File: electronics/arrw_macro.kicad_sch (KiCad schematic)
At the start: 23 parts, among them J7 Conn_01x05_Female, J8 Conn_01x05_Male, SW59 SW_SPST, SW60 SW_SPST, SW61 SW_SPST, SW62 SW_SPST, SW63 SW_SPST, SW64 SW_SPST, SW65 SW_SPST, SW66 SW_SPST, SW67 SW_SPST, SW68 SW_SPST, U4 PCA9675PW

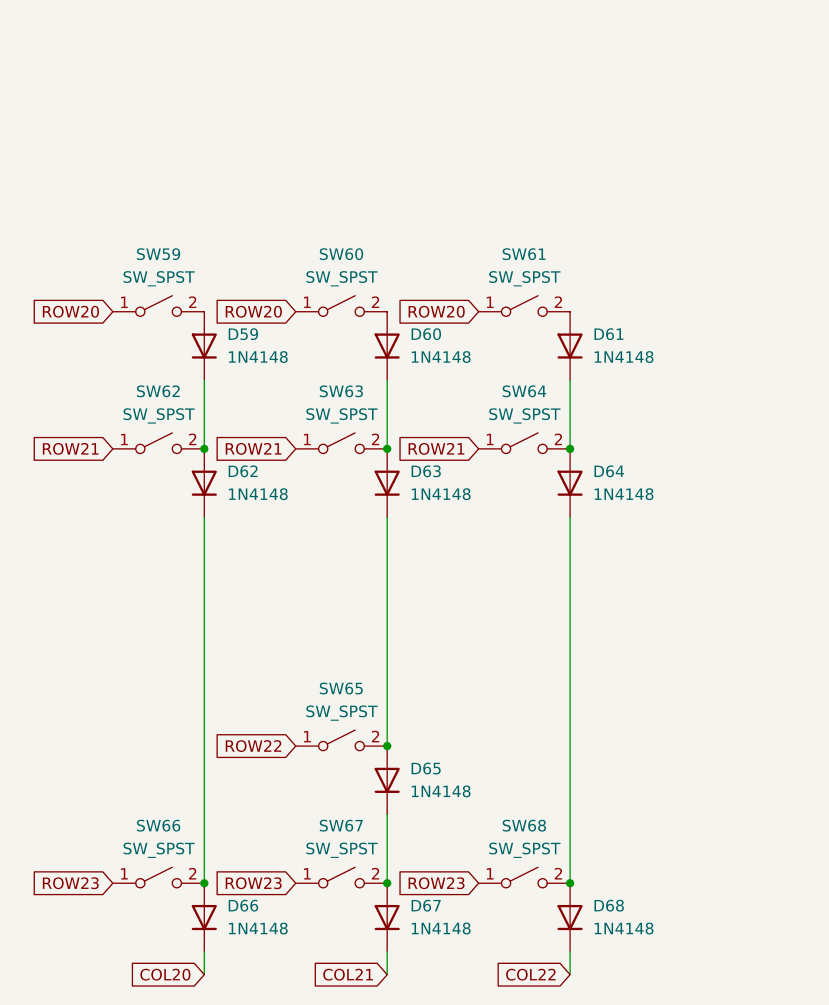
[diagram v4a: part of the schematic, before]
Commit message: fix arrow matrix
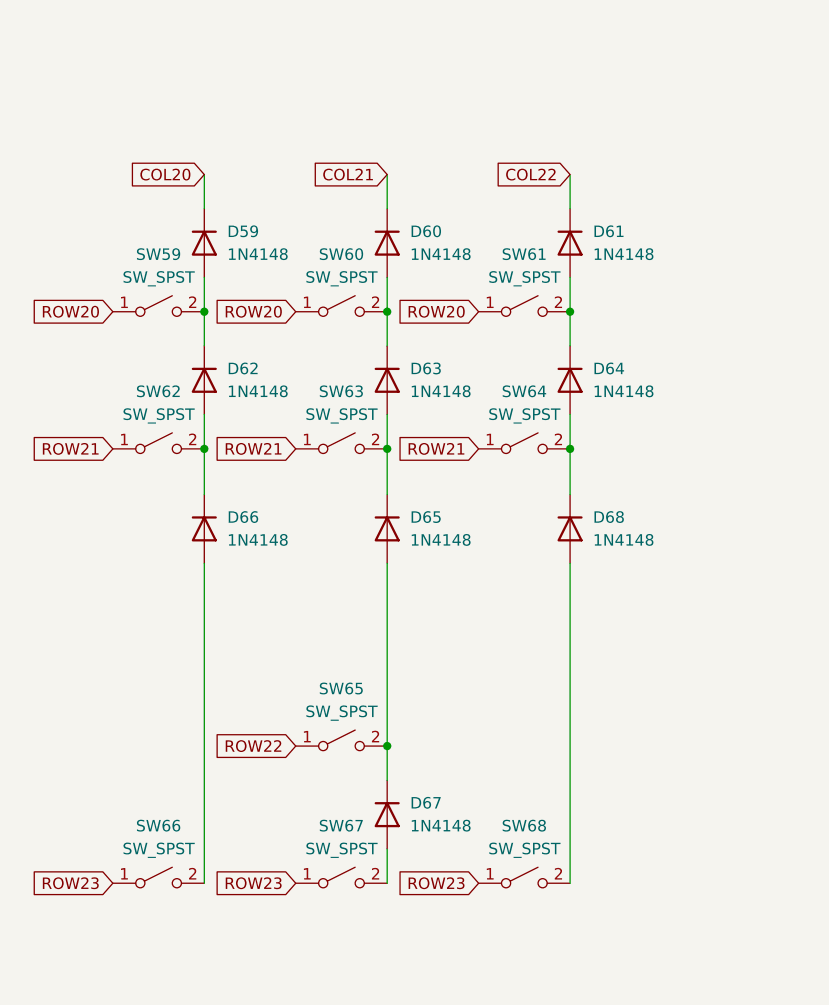
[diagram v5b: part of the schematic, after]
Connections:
- net COL20: now also D59.1 (K); no longer D66.1 (K)
- net COL21: now also D60.1 (K); no longer D67.1 (K)
- net COL22: now also D61.1 (K); no longer D68.1 (K)
- net at D65.2 (A), SW65.2 (B): now also D67.1 (K); no longer D63.1 (K)
- net at D67.2 (A), SW67.2 (B): no longer D65.1 (K)
- net at D63.2 (A), SW63.2 (B): now also D65.1 (K); no longer D60.1 (K)
- net at D60.2 (A), SW60.2 (B): now also D63.1 (K)
- net at D68.2 (A), SW68.2 (B): no longer D64.1 (K)
- net at D64.2 (A), SW64.2 (B): now also D68.1 (K); no longer D61.1 (K)
- net at D61.2 (A), SW61.2 (B): now also D64.1 (K)
- net at D59.2 (A), SW59.2 (B): now also D62.1 (K)
- net at D62.2 (A), SW62.2 (B): now also D66.1 (K); no longer D59.1 (K)
- net at D66.2 (A), SW66.2 (B): no longer D62.1 (K)
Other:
- moved on the sheet: D59, D60, D61, D62, D63, D64, D65, D66, D67, D68

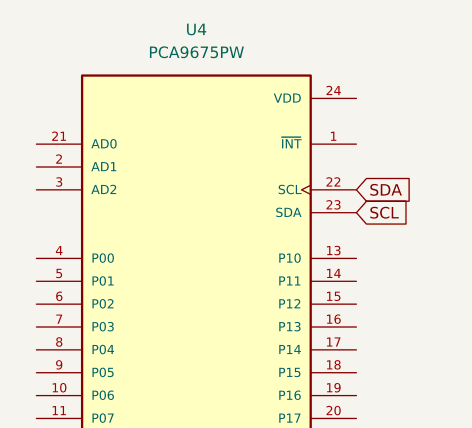
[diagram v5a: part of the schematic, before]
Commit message: fix arrow matrix
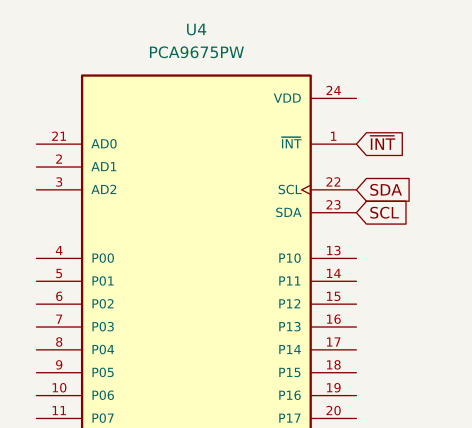
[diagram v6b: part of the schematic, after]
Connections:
- net ~{INT}: now also U4.1 (~{INT})
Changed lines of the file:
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@@
+    )
+  )
+  (global_label "~{INT}" (shape input) (at 224.79 41.91 0) (fields_autoplaced)
+    (effects (font (size 1.27 1.27)) (justify left))
+    (property "Intersheet References" "${INTERSHEET_REFS}" (id 0) (at 230.106 41.9894 0)
+      (effects (font (size 1.27 1.27)) (justify left) hide)
     )
   )

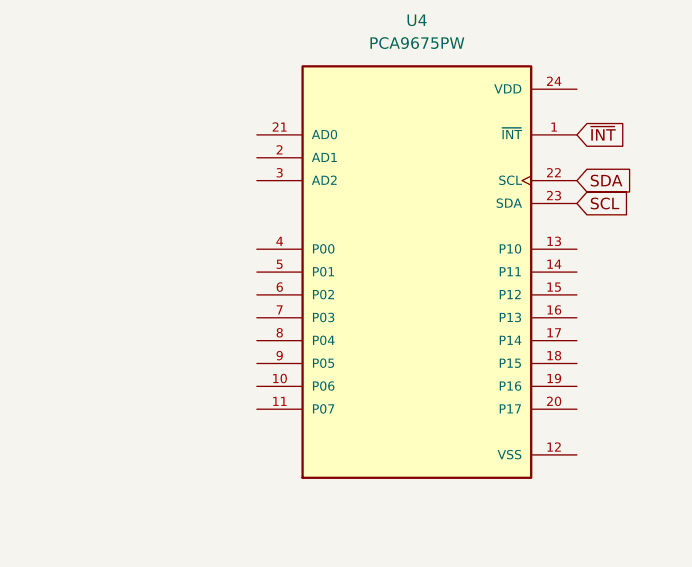
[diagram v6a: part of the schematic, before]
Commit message: connect matrix to io expander
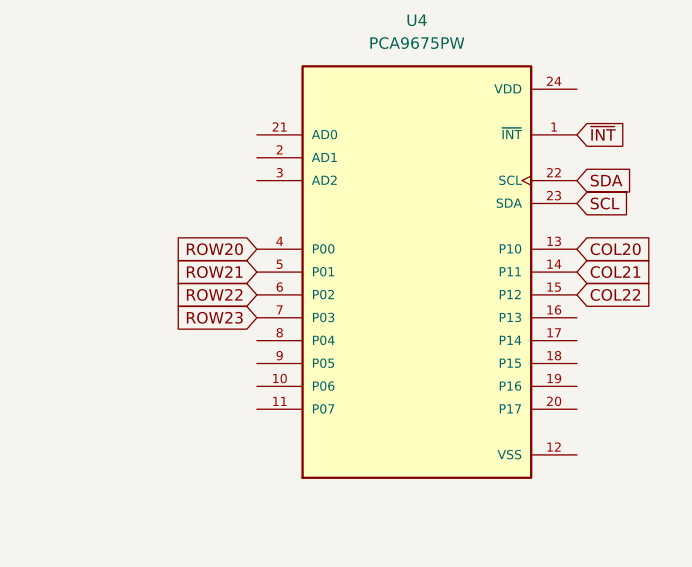
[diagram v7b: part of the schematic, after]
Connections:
- net COL20: now also U4.13 (P10)
- net COL21: now also U4.14 (P11)
- net COL22: now also U4.15 (P12)
- net ROW20: now also U4.4 (P00)
- net ROW21: now also U4.5 (P01)
- net ROW22: now also U4.6 (P02)
- net ROW23: now also U4.7 (P03)
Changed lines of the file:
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@@
     (stroke (width 0) (type default) (color 0 0 0 0))
+  )
+  (global_label "COL22" (shape input) (at 224.79 59.69 0) (fields_autoplaced)
+    (effects (font (size 1.27 1.27)) (justify left))
+    (property "Intersheet References" "${INTERSHEET_REFS}" (id 0) (at 233.2507 59.7694 0)
+      (effects (font (size 1.27 1.27)) (justify left) hide)
+    )
+  )
+  (global_label "ROW22" (shape input) (at 189.23 59.69 180) (fields_autoplaced)
+    (effects (font (size 1.27 1.27)) (justify right))
+    (property "Intersheet References" "${INTERSHEET_REFS}" (id 0) (at 180.3459 59.6106 0)
+      (effects (font (size 1.27 1.27)) (justify right) hide)
+    )
   )
   (global_label "SCL" (shape input) (at 223.52 119.38 0) (fields_autoplaced)
@@
     )
   )
+  (global_label "ROW23" (shape input) (at 189.23 62.23 180) (fields_autoplaced)
+    (effects (font (size 1.27 1.27)) (justify right))
+    (property "Intersheet References" "${INTERSHEET_REFS}" (id 0) (at 180.3459 62.1506 0)
+      (effects (font (size 1.27 1.27)) (justify right) hide)
+    )
+  )
   (global_label "ROW23" (shape input) (at 63.5 170.18 180) (fields_autoplaced)
     (effects (font (size 1.27 1.27)) (justify right))
     (property "Intersheet References" "${INTERSHEET_REFS}" (id 0) (at 54.6159 170.1006 0)
+      (effects (font (size 1.27 1.27)) (justify right) hide)
+    )
+  )
+  (global_label "ROW21" (shape input) (at 189.23 57.15 180) (fields_autoplaced)
+    (effects (font (size 1.27 1.27)) (justify right))
+    (property "Intersheet References" "${INTERSHEET_REFS}" (id 0) (at 180.3459 57.0706 0)
       (effects (font (size 1.27 1.27)) (justify right) hide)
     )
@@
     (property "Intersheet References" "${INTERSHEET_REFS}" (id 0) (at 54.6159 106.6006 0)
       (effects (font (size 1.27 1.27)) (justify right) hide)
+    )
+  )
+  (global_label "COL20" (shape input) (at 224.79 54.61 0) (fields_autoplaced)
+    (effects (font (size 1.27 1.27)) (justify left))
+    (property "Intersheet References" "${INTERSHEET_REFS}" (id 0) (at 233.2507 54.6894 0)
+      (effects (font (size 1.27 1.27)) (justify left) hide)
     )
   )
@@
     )
   )
+  (global_label "ROW20" (shape input) (at 189.23 54.61 180) (fields_autoplaced)
+    (effects (font (size 1.27 1.27)) (justify right))
+    (property "Intersheet References" "${INTERSHEET_REFS}" (id 0) (at 180.3459 54.5306 0)
+      (effects (font (size 1.27 1.27)) (justify right) hide)
+    )
+  )
   (global_label "SCL" (shape input) (at 224.79 49.53 0) (fields_autoplaced)
     (effects (font (size 1.27 1.27)) (justify left))
@@
       (effects (font (size 1.27 1.27)) (justify left) hide)
     )
+  )
+  (global_label "COL21" (shape input) (at 224.79 57.15 0) (fields_autoplaced)
+    (effects (font (size 1.27 1.27)) (justify left))
+    (property "Intersheet References" "${INTERSHEET_REFS}" (id 0) (at 233.2507 57.2294 0)
+      (effects (font (size 1.27 1.27)) (justify left) hide)
+    )

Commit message: finish matrix
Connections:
- net COL20: now also U4.15 (P12); no longer U4.13 (P10)
- net COL22: now also U4.13 (P10); no longer U4.15 (P12)
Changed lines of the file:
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@@
     (stroke (width 0) (type default) (color 0 0 0 0))
-  )
-  (global_label "COL22" (shape input) (at 224.79 59.69 0) (fields_autoplaced)
-    (effects (font (size 1.27 1.27)) (justify left))
-    (property "Intersheet References" "${INTERSHEET_REFS}" (id 0) (at 233.2507 59.7694 0)
-      (effects (font (size 1.27 1.27)) (justify left) hide)
-    )
   )
   (global_label "ROW22" (shape input) (at 189.23 59.69 180) (fields_autoplaced)
@@
     (property "Intersheet References" "${INTERSHEET_REFS}" (id 0) (at 54.6159 121.8406 0)
       (effects (font (size 1.27 1.27)) (justify right) hide)
+    )
+  )
+  (global_label "COL21" (shape input) (at 224.79 57.15 0) (fields_autoplaced)
+    (effects (font (size 1.27 1.27)) (justify left))
+    (property "Intersheet References" "${INTERSHEET_REFS}" (id 0) (at 233.2507 57.0706 0)
+      (effects (font (size 1.27 1.27)) (justify left) hide)
     )
   )
@@
     )
   )
+  (global_label "COL20" (shape input) (at 224.79 59.69 0) (fields_autoplaced)
+    (effects (font (size 1.27 1.27)) (justify left))
+    (property "Intersheet References" "${INTERSHEET_REFS}" (id 0) (at 233.2507 59.6106 0)
+      (effects (font (size 1.27 1.27)) (justify left) hide)
+    )
+  )
   (global_label "ROW21" (shape input) (at 104.14 121.92 180) (fields_autoplaced)
     (effects (font (size 1.27 1.27)) (justify right))
@@
     (property "Intersheet References" "${INTERSHEET_REFS}" (id 0) (at 54.6159 106.6006 0)
       (effects (font (size 1.27 1.27)) (justify right) hide)
-    )
-  )
-  (global_label "COL20" (shape input) (at 224.79 54.61 0) (fields_autoplaced)
-    (effects (font (size 1.27 1.27)) (justify left))
-    (property "Intersheet References" "${INTERSHEET_REFS}" (id 0) (at 233.2507 54.6894 0)
-      (effects (font (size 1.27 1.27)) (justify left) hide)
     )
   )
@@
     )
   )
-  (global_label "COL21" (shape input) (at 224.79 57.15 0) (fields_autoplaced)
-    (effects (font (size 1.27 1.27)) (justify left))
-    (property "Intersheet References" "${INTERSHEET_REFS}" (id 0) (at 233.2507 57.2294 0)
-      (effects (font (size 1.27 1.27)) (justify left) hide)
-    )
-  )
   (global_label "ROW23" (shape input) (at 104.14 170.18 180) (fields_autoplaced)
     (effects (font (size 1.27 1.27)) (justify right))
@@
       (effects (font (size 1.27 1.27)) (justify left) hide)
     )
+  )
+  (global_label "COL22" (shape input) (at 224.79 54.61 0) (fields_autoplaced)
+    (effects (font (size 1.27 1.27)) (justify left))
+    (property "Intersheet References" "${INTERSHEET_REFS}" (id 0) (at 233.2507 54.5306 0)
+      (effects (font (size 1.27 1.27)) (justify left) hide)
+    )
